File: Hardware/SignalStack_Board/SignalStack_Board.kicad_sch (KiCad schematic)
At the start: 67 parts, among them J1 Molex_uF_SV_06, J2 RJ45_LED_Shielded, Q1 SI4156DY, Q10 BSS138, Q11 BSS138, Q12 BSS138, Q2 SI4156DY, Q3 SI4156DY, Q4 SI4156DY, Q5 SI4156DY, Q6 SI4156DY, Q7 SI4156DY, Q8 SI4156DY, Q9 BSS138, U1 OKI, U2 Teensy4.1_DEV-16771, U3 IRS2005S, U4 IRS2005S, U5 IRS2005S, U6 IRS2005S, U7 MMC5633NJL, U8 SMAJ12CA

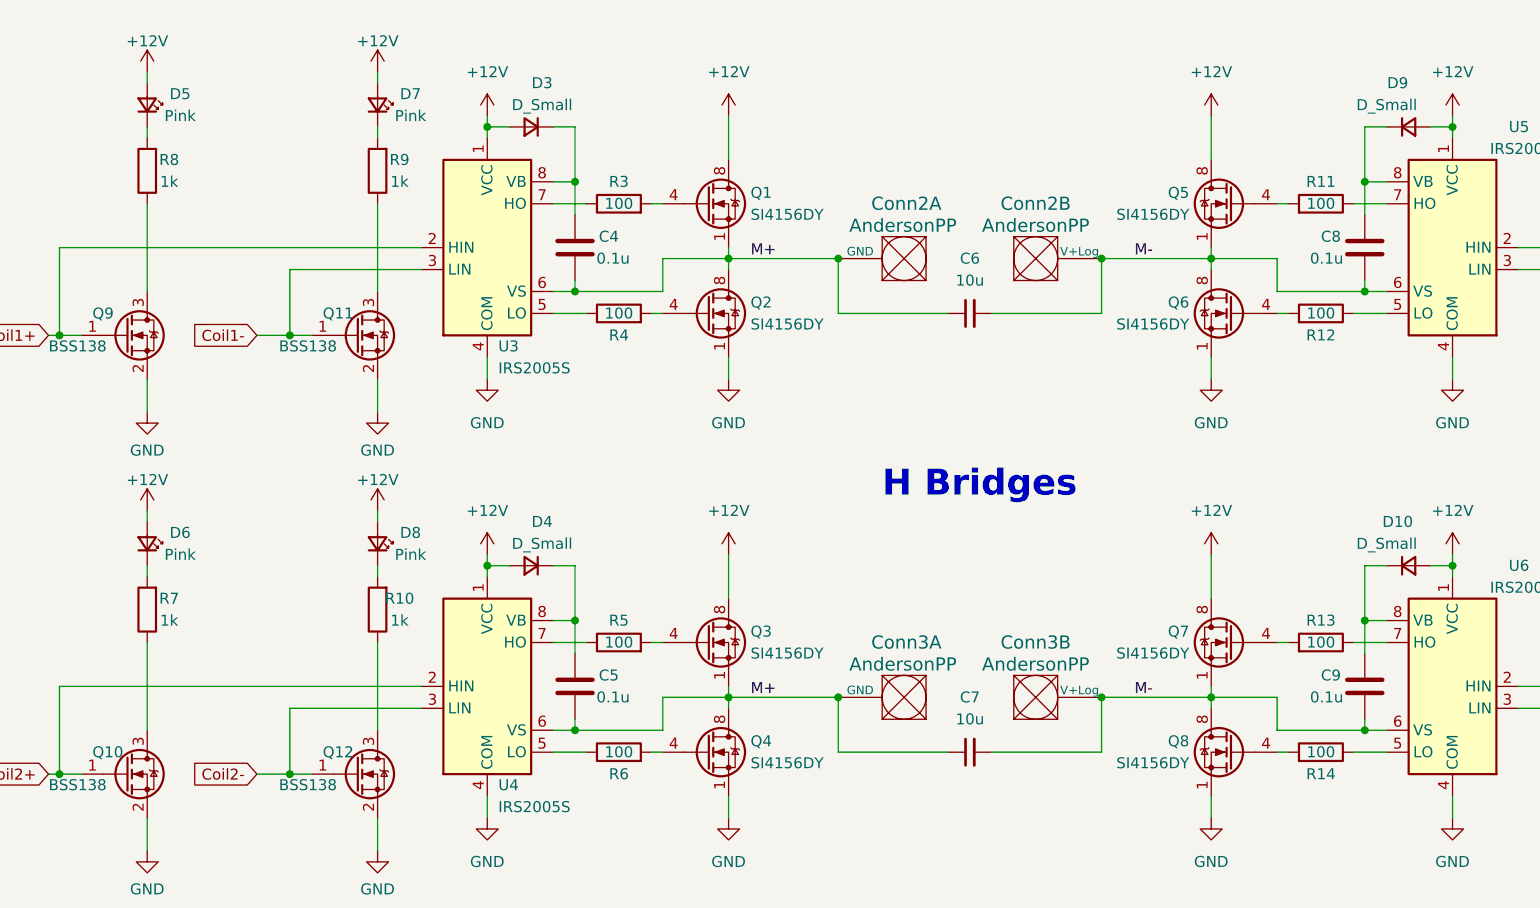
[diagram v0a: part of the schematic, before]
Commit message: Light schematic cleaning
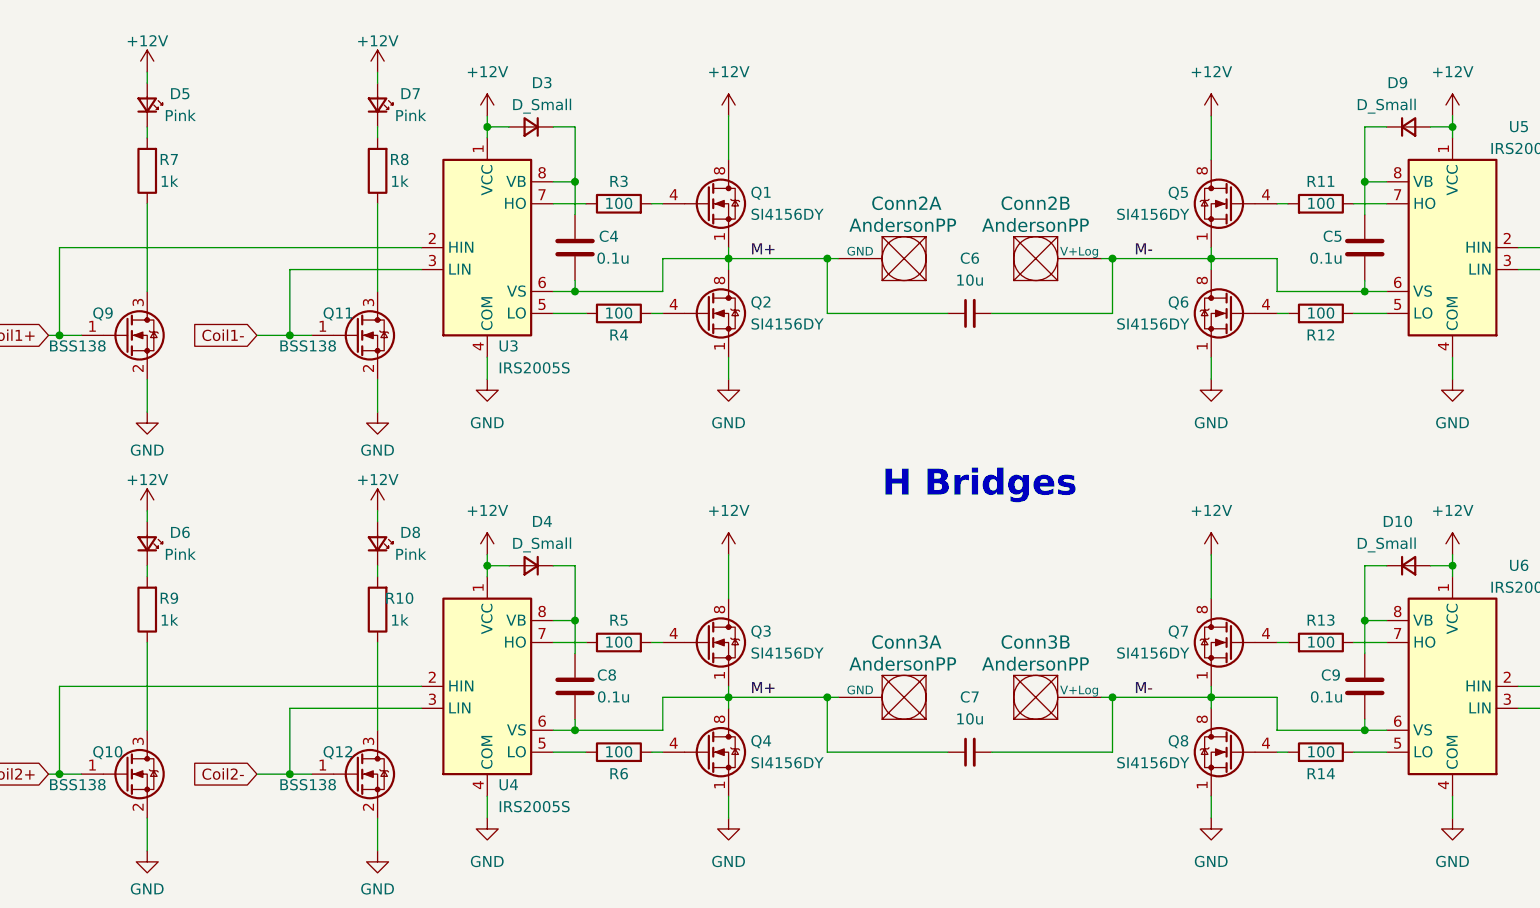
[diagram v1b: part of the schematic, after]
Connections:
- net M+: now also C8.2; no longer C5.2
- net M-: now also C5.2; no longer C8.2
- net at D9.1 (K), U5.8 (VB): now also C5.1; no longer C8.1
- net at D5.1 (K): now also R7.2; no longer R8.2
- net at D7.1 (K): now also R8.2; no longer R9.2
- net at D4.1 (K), U4.8 (VB): now also C8.1; no longer C5.1
- net at R8.1: now also Q11.3 (D); no longer Q9.3 (D)
- net at D6.1 (K): now also R9.2; no longer R7.2
- net at R9.1: now also Q10.3 (D); no longer Q11.3 (D)
- net at R7.1: now also Q9.3 (D); no longer Q10.3 (D)
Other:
- moved on the sheet: C5, C8, R7, R8, R9

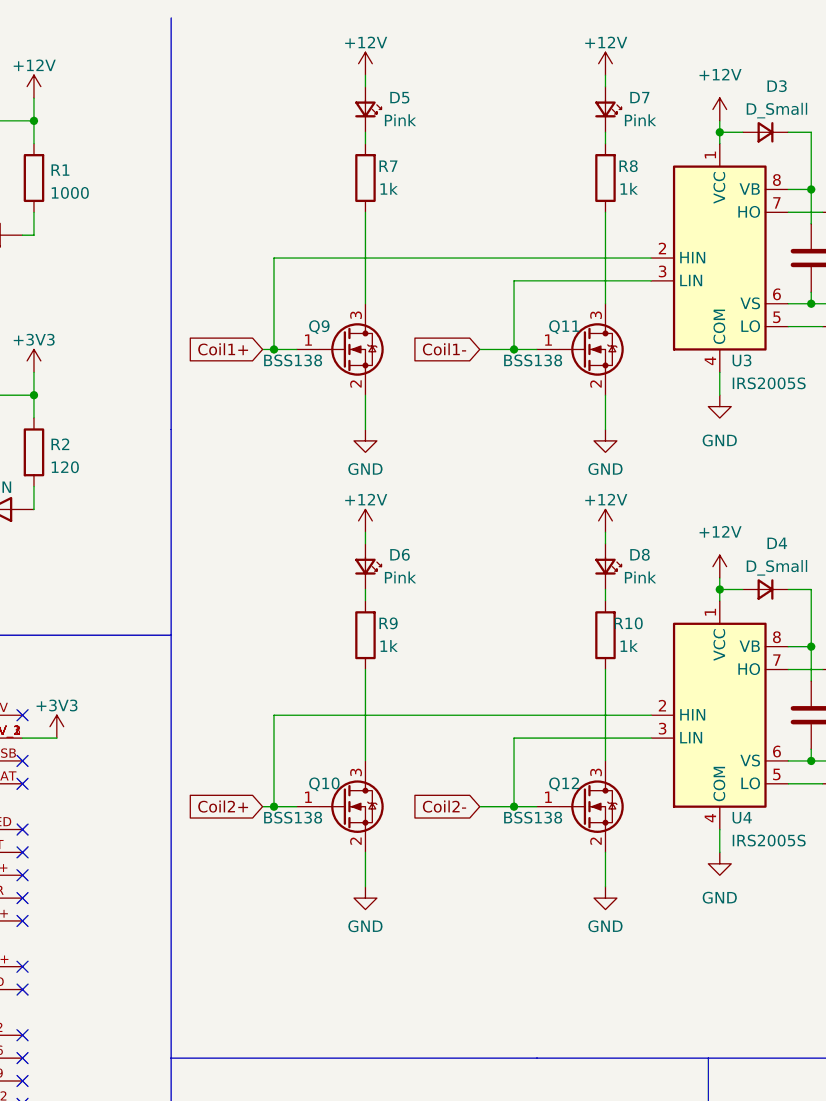
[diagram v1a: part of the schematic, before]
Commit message: Changed H Bridge LEDs
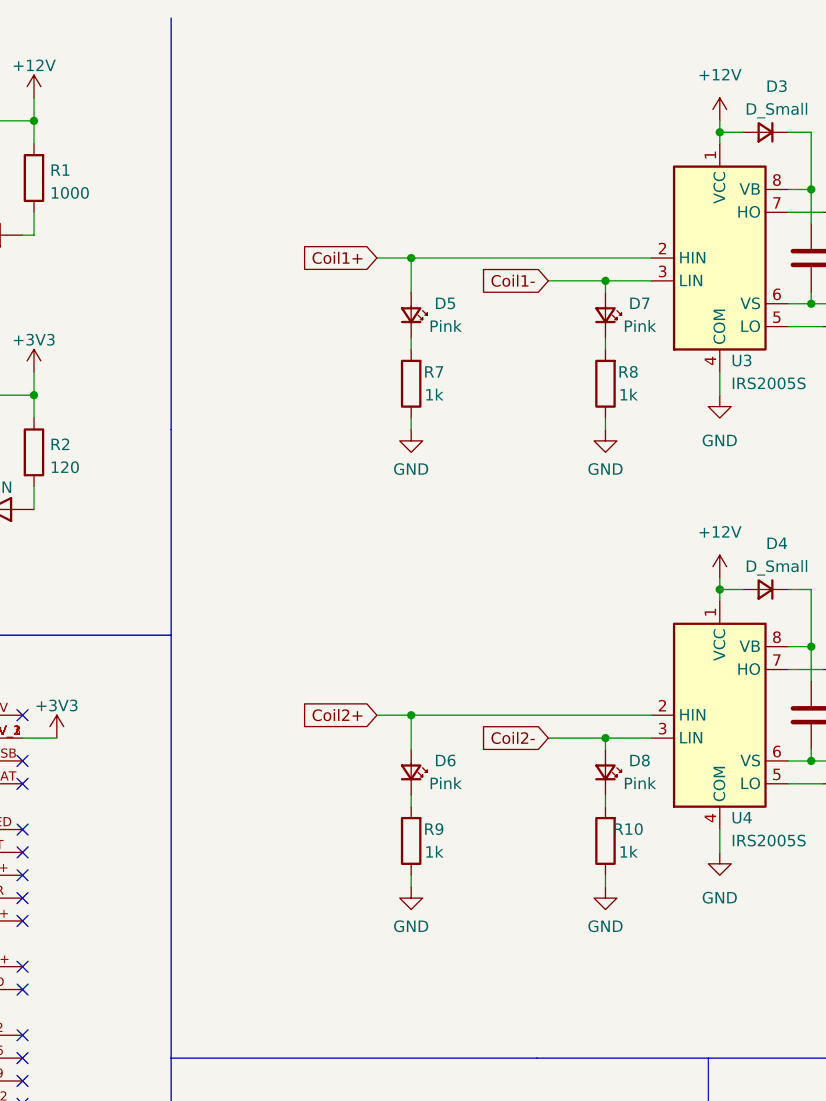
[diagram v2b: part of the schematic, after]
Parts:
- removed Q10, Q11, Q12, Q9: BSS138, Package_TO_SOT_SMD:SOT-23, symbol Transistor_FET:BSS138
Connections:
- net +12V: no longer D5.2 (A), D6.2 (A), D7.2 (A), D8.2 (A)
- net Coil1+: now also D5.2 (A)
- net Coil1-: now also D7.2 (A)
- net Coil2+: now also D6.2 (A)
- net Coil2-: now also D8.2 (A)
- net GND: now also R10.1, R7.1, R8.1, R9.1
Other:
- moved on the sheet: D5, D6, D7, D8, R10, R7, R8, R9

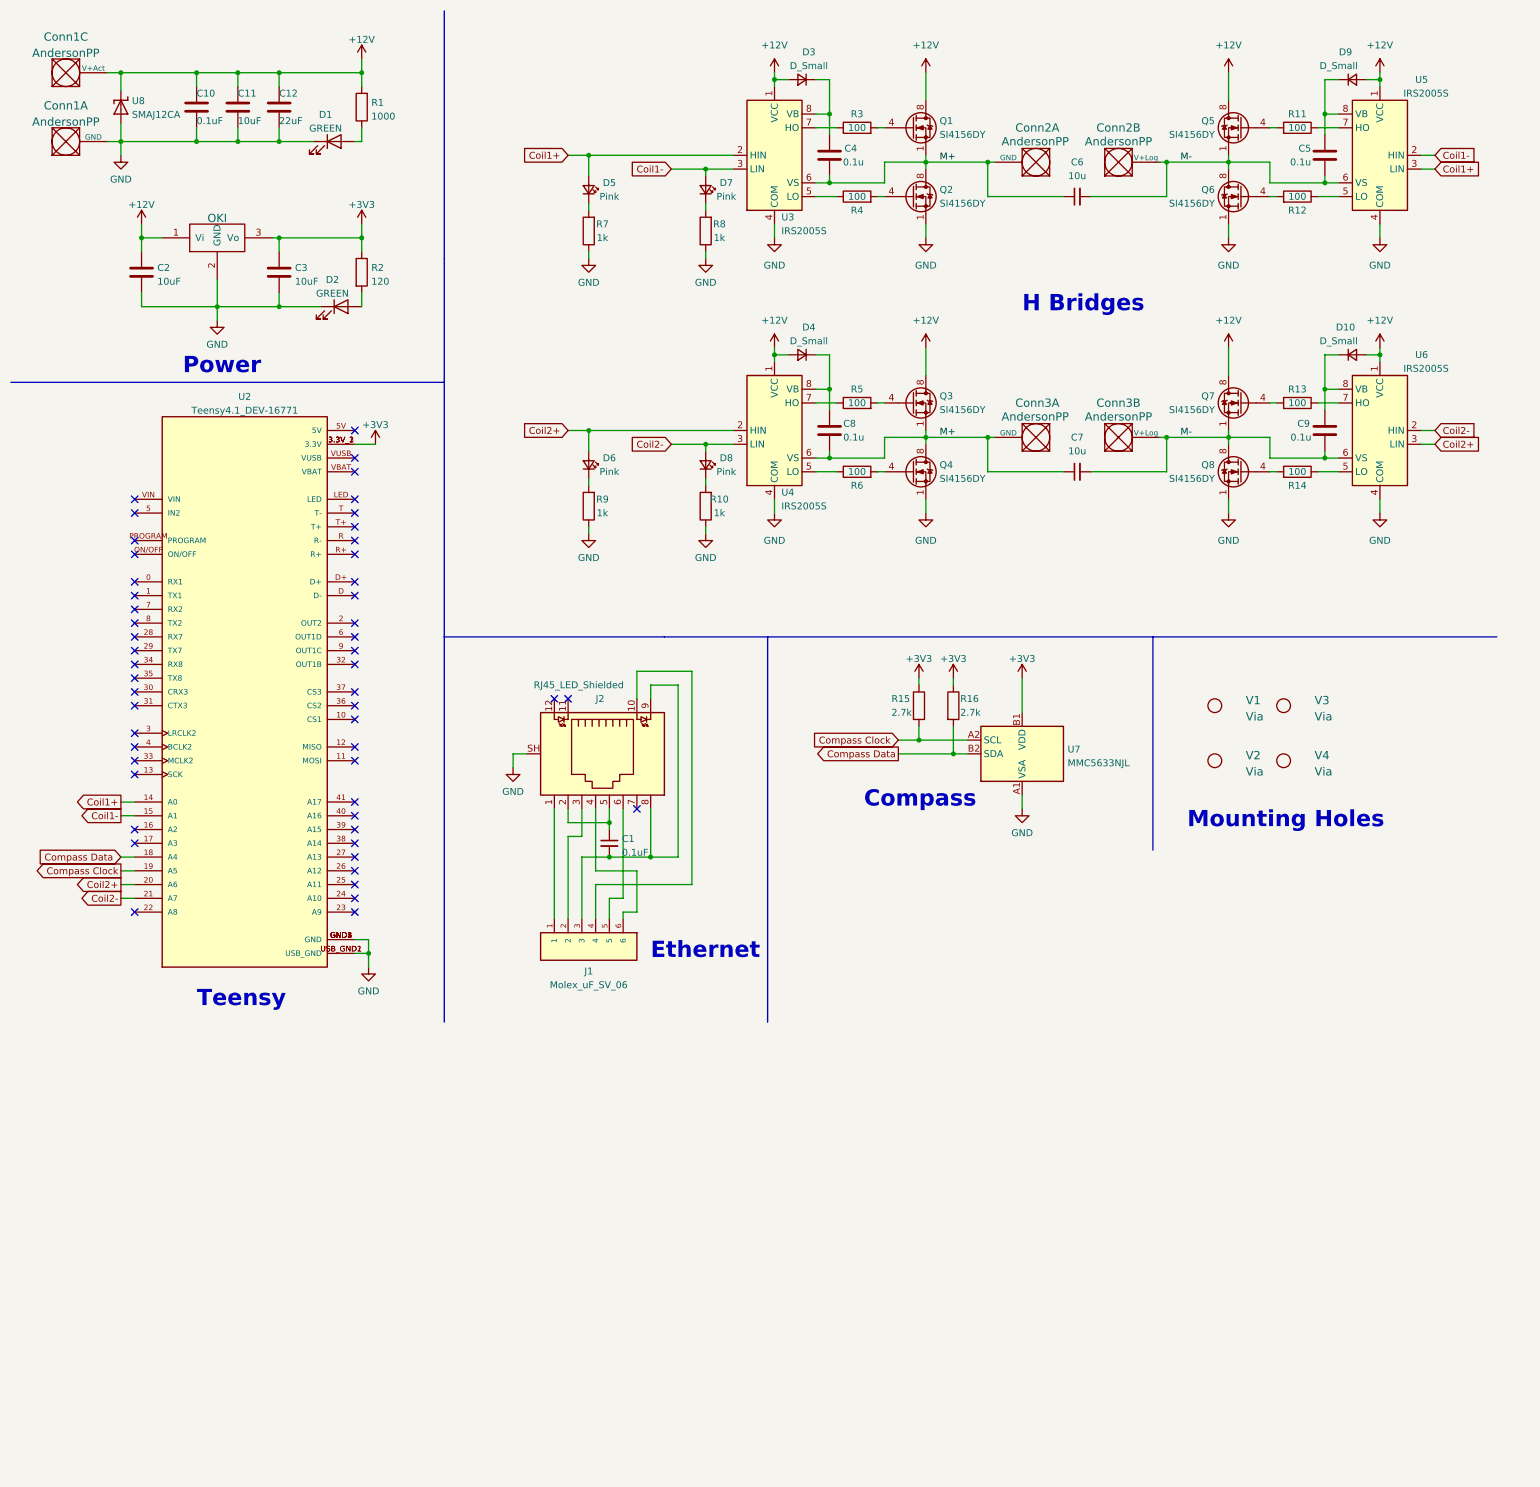
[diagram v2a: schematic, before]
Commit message: Fixed LED resistances
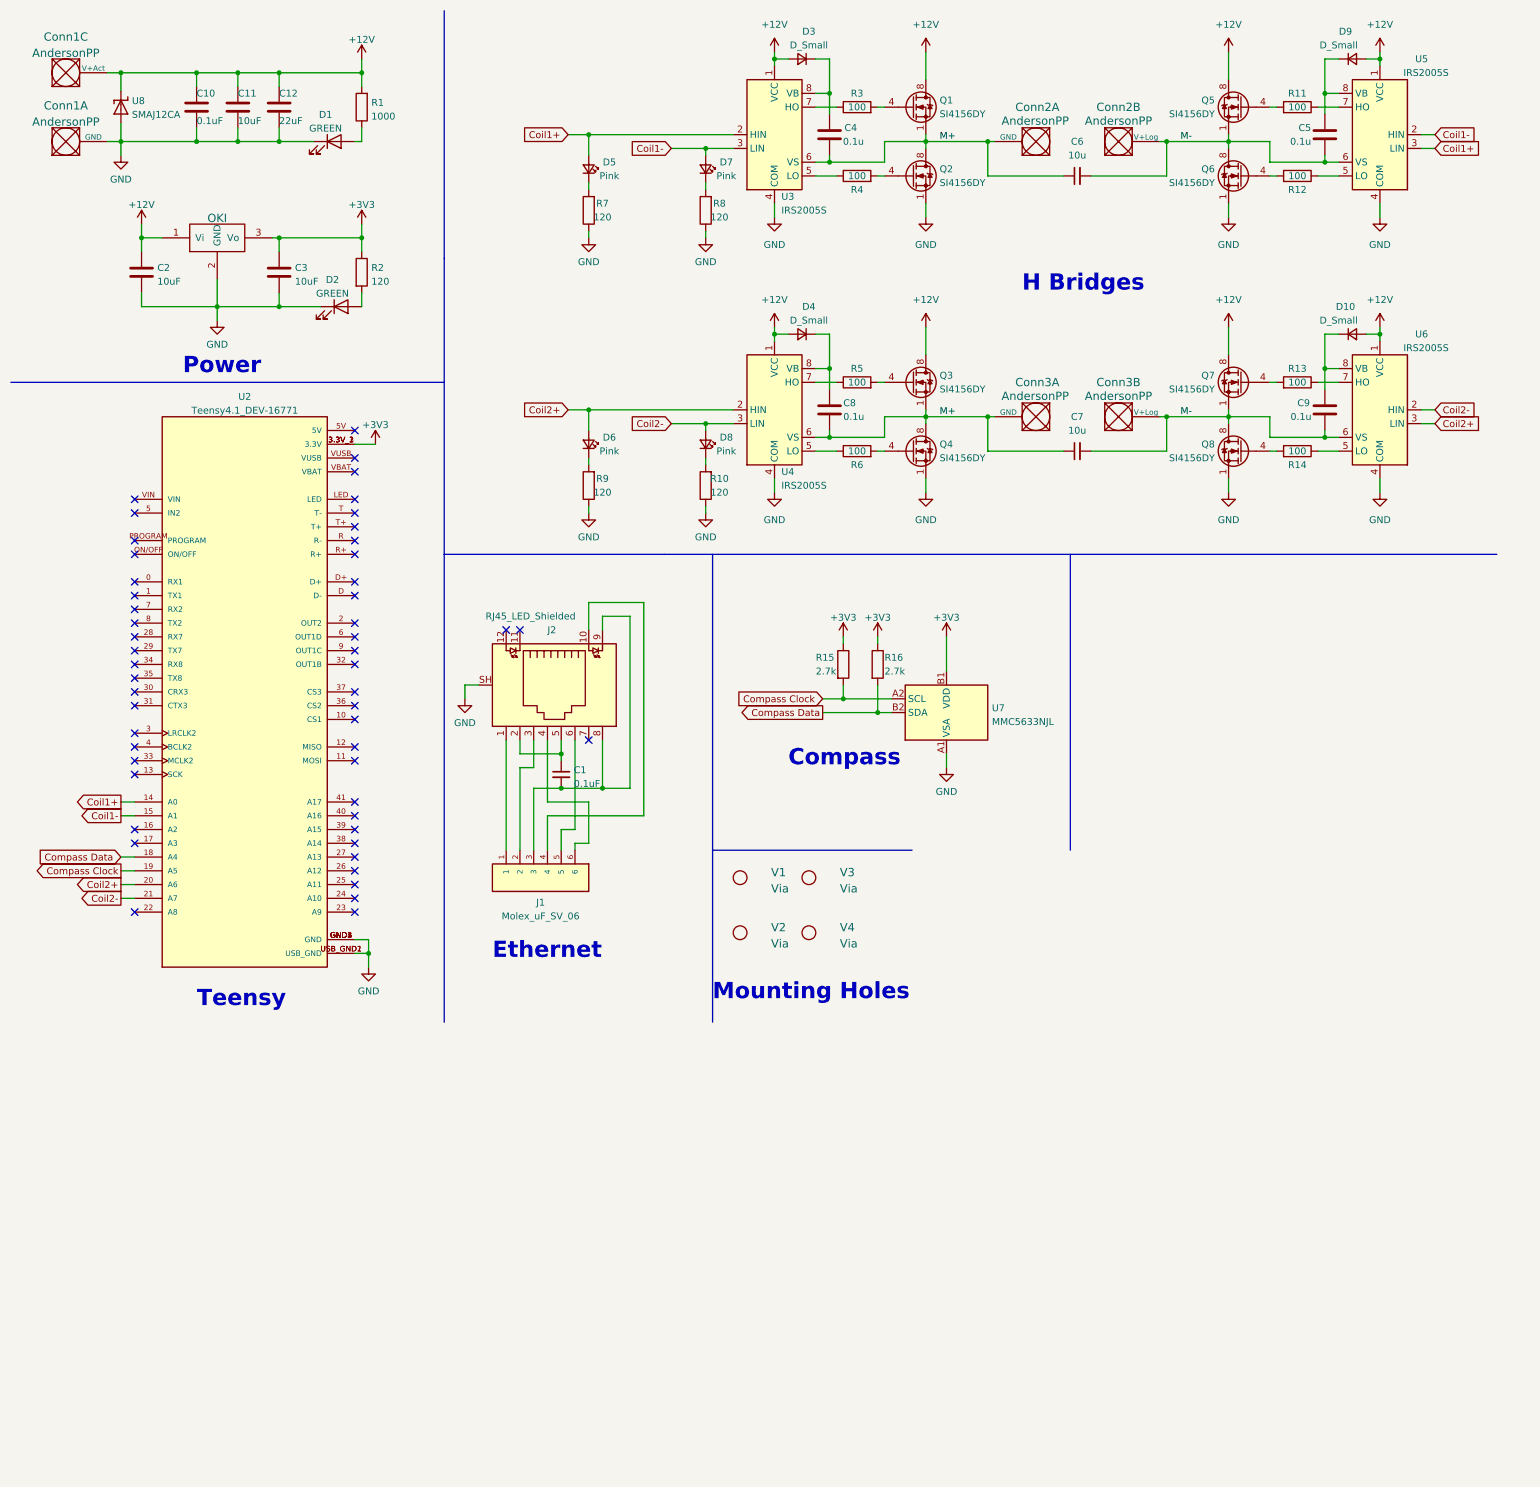
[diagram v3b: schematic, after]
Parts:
- R10, R7, R8, R9: value 1k -> 120
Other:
- moved on the sheet: C1, C4, C5, C6, C7, C8, C9, Conn2A, Conn2B, Conn3A, Conn3B, D10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
